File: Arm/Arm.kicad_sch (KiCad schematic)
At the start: 53 parts, among them J10 SparkMAX XT60 F, J11 CAN OUT, J12 Axis 0, J13 SparkMAX XT60 F, J14 Encoder 0, J2 Encoder Bundle, J3 CAN IN, J4 5V Swtich Power, J5 Power IN XT60 M, J6 SparkMAX XT60 F, J7 Power OUT XT60 F, J8 Lynx, J9 CANBUS, M1 Fan, U4 TJA1051T, U5 TJA1051T, U7 RASPBERRY_PI_4B_4GB

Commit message: URC '25 - V2
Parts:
- removed A1, A2: Adafruit_Feather_HUZZAH32_ESP32, Module:Adafruit_Feather, symbol Arm:Adafruit Feather ESP32 V2
- removed J12: Axis 0, Connector_Molex:Molex_Mini-Fit_Jr_5566-04A_2x02_P4.20mm_Vertical, symbol Connector:Conn_01x04_Pin
- removed U6: ~, Arm:Pololu 3730, symbol Arm:Pololu_3730
- added C7: 0.1 uF, Capacitor_SMD:C_0603_1608Metric_Pad1.08x0.95mm_HandSolder, symbol Device:C
- added D5: Inolux_IN-PI554FCH, LED_SMD:LED_Inolux_IN-PI554FCH_PLCC4_5.0x5.0mm_P3.2mm, symbol LED:Inolux_IN-PI554FCH
- added J12: SparkMAX XT60 F, Connector_AMASS:AMASS_XT60-F_1x02_P7.20mm_Vertical, symbol Connector:Conn_01x02_Pin
- added R16: 10K ohm, Resistor_SMD:R_0603_1608Metric_Pad0.98x0.95mm_HandSolder, symbol Device:R
- added U6, U8: ~, ESP 32 DOIT devkit V1:esp32_devkit_v1_doit, symbol ESP 32 DOIT devkit V1:ESP32_DOIT_devkit_V1
- J8: footprint Connector_Molex:Molex_Mini-Fit_Jr_5566-04A_2x02_P4.20mm_Vertical -> Connector_AMASS:AMASS_XT30U-F_1x02_P5.0mm_Vertical; symbol Connector:Conn_01x04_Pin -> Connector:Conn_01x02_Pin
- R5: value 3.8K Ohm -> 3.32K Ohm
- R7: value 3.1K Ohm -> 2.21K ohm
- U7: footprint Raspi:MODULE_RASPBERRY_PI_4B_4GB -> RASPBERRY_PI_4B_4GB:MODULE_RASPBERRY_PI_4B_4GB; Description_1 BCM2711 Raspberry Pi 4 Model B 4GB - ARM® Cortex®-A72 MPU Embedded Evaluation Board -> BCM2711 Raspberry Pi 4 Model B 4GB - ARM® Cortex®-A72 MPU Embedded Evaluation Board
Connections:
- net ESP_RX-LYNX_TX is gone; now on net +12V: J8.1 (Pin_1)
- net ESP_TX-LYNX_RX is gone; now on net GND: J8.2 (Pin_2)
- net +12V: no longer J8.3 (Pin_3)
- net +3.3V: now also R16.1; no longer R3.1
- net +5V: now also C7.1, D5.3 (VDD), U6.15 (VIN), U8.15 (VIN)
- net +BATT: now also J12.2 (Pin_2)
- net 12V_ADC: now also U6.2 (GPI36/A0)
- net 5V_ADC: now also U6.4 (GPI34/A6)
- net BATT_ADC: now also U6.3 (GPI39/A3)
- net CLK_ESP0: now also U6.24 (GPIO18/SCK)
- net CS_Encoder_0: now also J14.3 (Pin_3), U6.6 (GPIO32/A4); no longer J14.4 (Pin_4)
- net CS_Encoder_1: now also U6.7 (GPIO33/A5)
- net CS_Encoder_2: now also U6.8 (GPIO25/A18)
- net CS_Encoder_3: now also U6.9 (GPIO26/A19)
- net ESP0 3.3V: now also U6.16 (3.3V)
- net ESP0_ESP1_SERIAL: now also U6.21 (GPIO16/RX2), U8.22 (GPIO17/TX2)
- net ESP1 3.3V: now also U8.16 (3.3V)
- net ESP1_ESP0_SERIAL: now also U6.22 (GPIO17/TX2), U8.21 (GPIO16/RX2)
- net GND: now also J14.2 (Pin_2), C7.2, D5.1 (VSS), J12.1 (Pin_1), U6.14 (GND), U6.17 (GND), U8.14 (GND), U8.17 (GND); no longer J14.5 (Pin_5), J8.4 (Pin_4)
- net MISO_ESP0: now also J14.5 (Pin_5), U6.25 (GPIO19/MISO); no longer J14.3 (Pin_3)
- net MOSI_ESP0: now also J14.4 (Pin_4), U6.30 (GPIO23/MOSI); no longer J14.2 (Pin_2)
- net ESP0_RX-CAN_TX renamed ESP0_TX-CAN_TX
- net ESP0_TX-CAN_TX: now also U6.13 (GPIO13/A14)
- net ESP0_TX-CAN_RX renamed ESP0_RX-CAN_RX
- net ESP0_RX-CAN_RX: now also U6.11 (GPIO14/A16)
- net ESP1_RX-CAN_TX renamed ESP1_TX-CAN_TX
- net ESP1_TX-CAN_TX: now also U8.13 (GPIO13/A14)
- net ESP1_TX-CAN_RX renamed ESP1_RX-CAN_RX
- net ESP1_RX-CAN_RX: now also U8.11 (GPIO14/A16)
- new net 3.3V_ADC: R16.2, R3.1, U6.5 (GPI35/A7)
- new net LED Debug: D5.2 (DIN), U6.29 (GPIO22/SCL)
- no-connect marks 41 -> 73
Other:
- note added: "Status LED"
- note removed: "Axis 0 Motor Driver"
- note removed: "Stepper Motor Axis 0"
- note removed: "Supply 14.8V Max Current 1.5A"

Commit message: PCB Layout....
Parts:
- removed C2: 4.7 nf, Capacitor_SMD:C_0603_1608Metric_Pad1.08x0.95mm_HandSolder, symbol Device:C
- removed R12, R13: 60Ω, Resistor_SMD:R_0603_1608Metric_Pad0.98x0.95mm_HandSolder, symbol Device:R_Small_US
- removed U5: TJA1051T, Package_SO:SOIC-8_3.9x4.9mm_P1.27mm, symbol Interface_CAN_LIN:TJA1051T-3
- removed U6, U8: ~, ESP 32 DOIT devkit V1:esp32_devkit_v1_doit, symbol ESP 32 DOIT devkit V1:ESP32_DOIT_devkit_V1
- removed U7: RASPBERRY_PI_4B_4GB, RASPBERRY_PI_4B_4GB:MODULE_RASPBERRY_PI_4B_4GB, symbol RASPBERRY_PI_4B_4GB:RASPBERRY_PI_4B_4GB
- added C10, C8, C9: 0.1 uF, Capacitor_SMD:C_0603_1608Metric_Pad1.08x0.95mm_HandSolder, symbol Device:C
- added C11: 4.7 nF, Capacitor_SMD:C_0603_1608Metric_Pad1.08x0.95mm_HandSolder, symbol Device:C
- added R17, R18: 60Ω, Resistor_SMD:R_0603_1608Metric_Pad0.98x0.95mm_HandSolder, symbol Device:R_Small_US
- added U5: ESP32-S3-DevKitC, Astra Lib:ESP32-S3-DevKitC, symbol ESP32-S3-DevkitC:ESP32-S3-DevKitC
- added U9: MCP251863T-E-9PX, Package_DFN_QFN:VQFN-28-1EP_5x5mm_P0.5mm_EP3.25x3.25mm, symbol Interface_CAN_LIN:MCP251863T-E-9PX
- added Y3: 40Mhz Crystal, Crystal:Crystal_SMD_3225-4Pin_3.2x2.5mm, symbol Device:Crystal_GND23
- C4: value 1 uF -> 13 pF
- C6: value 0.1 uF -> 13 pF
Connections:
- net +5V: now also C10.2, U5.3 (CHIP_PU), U9.13 (VCC); no longer C4.1
- net 12V_ADC: now also U5.31 (GPIO0)
- net 3.3V_ADC: now also U5.13 (GPIO3/ADC1_CH2)
- net 5V_ADC: now also U5.40 (GPIO2/ADC1_CH1)
- net Arm Motor CAN+: now also R18.2, U9.17 (CANH)
- net Arm Motor CAN-: now also R17.1, U9.16 (CANL)
- net BATT_ADC: now also U5.41 (GPIO1/ADC1_CH0)
- net CLK_ESP0: now also U5.29 (GPIO48), U9.22 (SCK)
- net CS_Encoder_0: now also U5.34 (GPIO37)
- net CS_Encoder_1: now also U5.35 (GPIO38)
- net CS_Encoder_2: now also U5.30 (GPIO45)
- net CS_Encoder_3: now also U5.14 (GPIO46)
- net ESP0 3.3V: now also C8.1, C9.1, U5.1 (3V3), U5.2 (3V3), U9.14 (VIO), U9.26 (VDD)
- net ESP0_RX-CAN_RX: now also U5.7 (GPIO7/ADC1_CH6)
- net ESP0_TX-CAN_TX: now also U5.11 (GPIO18/ADC2_CH7)
- net GND: now also C4.1, C10.1, C11.1, C8.2, C9.2, U5.22 (GND), U5.23 (GND), U5.24 (GND), U5.44 (GND), U9.10 (GND), U9.7 (VSS), Y3.2, Y3.3; no longer C4.2
- net LED Debug: now also U5.27 (GPIO21)
- net MISO_ESP0: now also U5.28 (GPIO47), U9.23 (SDI)
- net MOSI_ESP0: now also U5.32 (GPIO35), U9.24 (SDO)
- net ESP1 3.3V: no longer names the net of C6.2
- net ESP1 3.3V: now also U9.4 (OSC2), Y3.1
- new net: C4.2, U9.5 (OSC1), Y3.4
- new net: C11.2, R17.2, R18.1
- new net: U9.1 (RXCAN), U9.11 (RXD)
- new net: U9.20 (TXD), U9.28 (TXCAN)
- new net CS_Motor_CAN: U5.33 (GPIO36), U9.25 (~{CS})
- no-connect marks 73 -> 14
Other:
- note added: "Main ESP"
- note removed: "Motor Control"
- note removed: "Nuc Control"
- note removed: "Raspberry Pi"
- moved on the sheet: C1, C3, C5, C7, D1, D2, D3, D4, D5, H1, H2, H3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

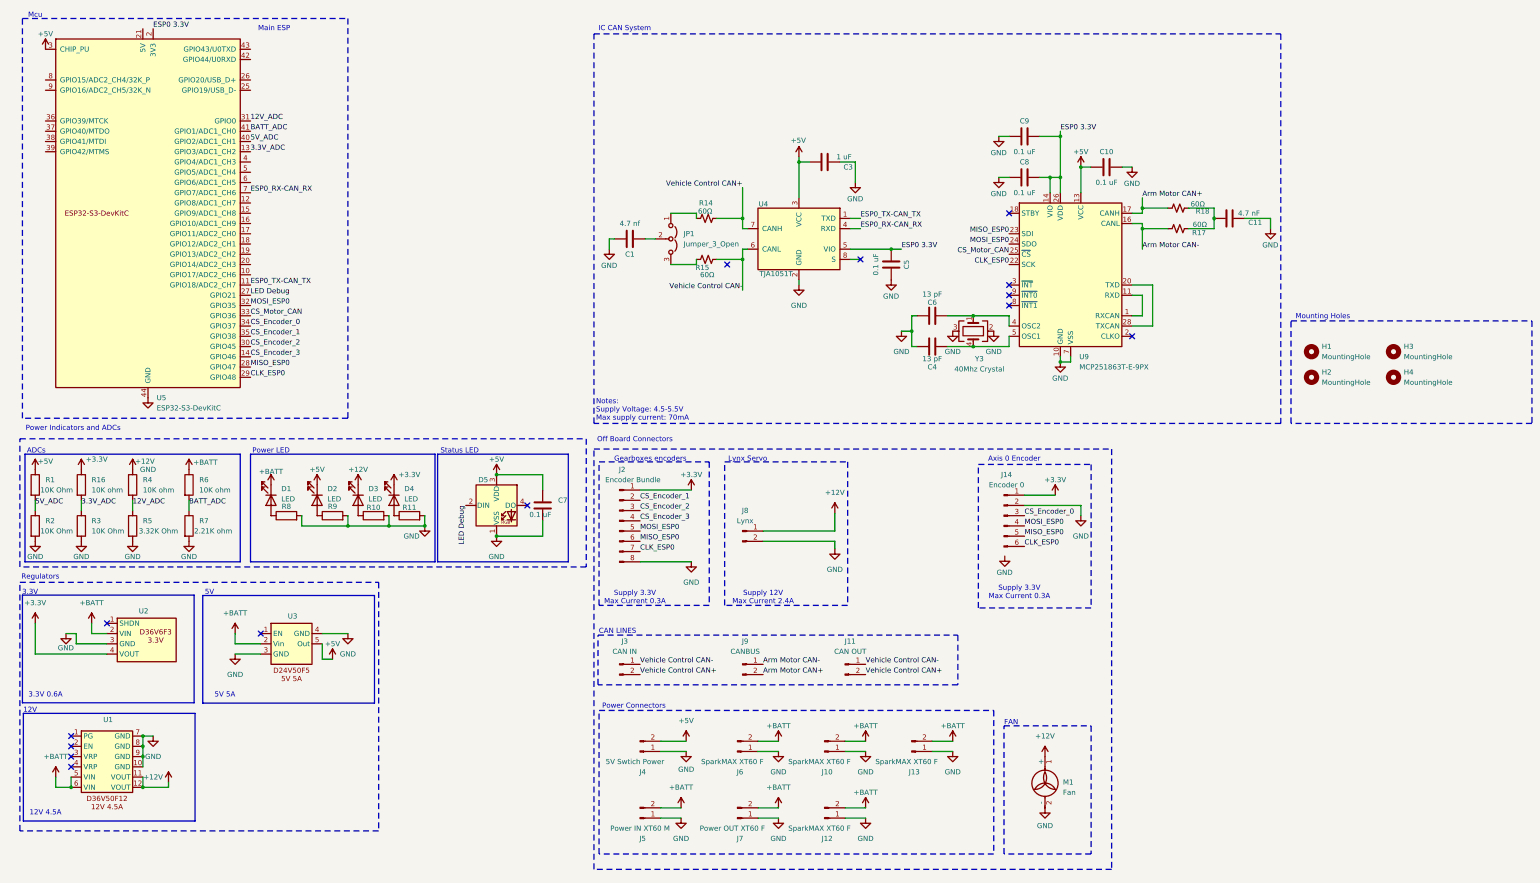
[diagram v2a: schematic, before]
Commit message: Progrss on socket -FeedBack Fixes -PCB Layout and signal routing
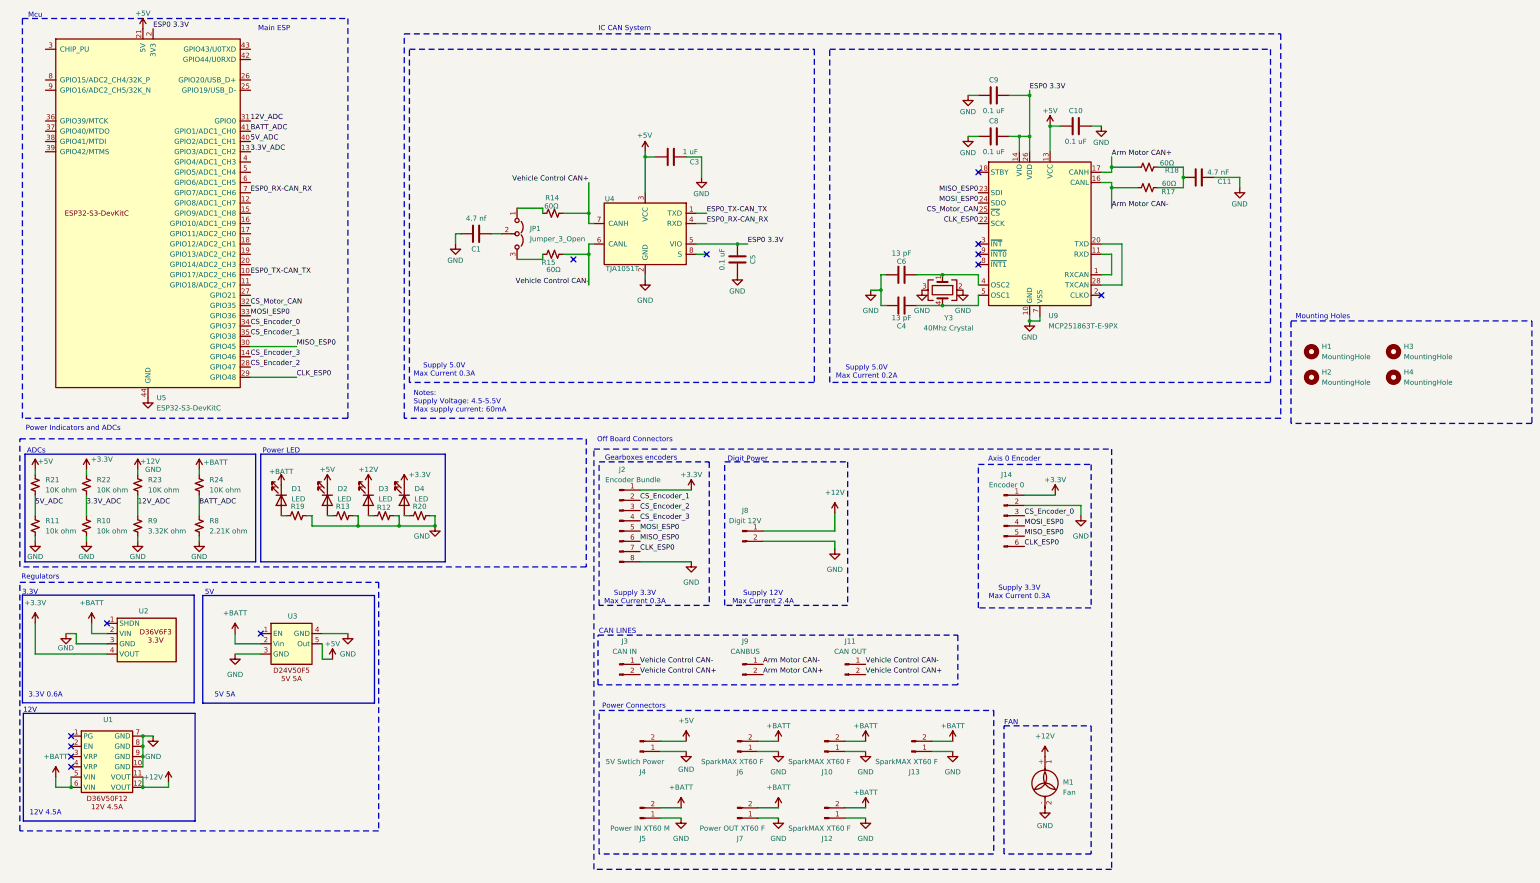
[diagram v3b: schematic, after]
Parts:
- removed C7: 0.1 uF, Capacitor_SMD:C_0603_1608Metric_Pad1.08x0.95mm_HandSolder, symbol Device:C
- removed D5: Inolux_IN-PI554FCH, LED_SMD:LED_Inolux_IN-PI554FCH_PLCC4_5.0x5.0mm_P3.2mm, symbol LED:Inolux_IN-PI554FCH
- removed R1, R2, R3: 10K Ohm, Resistor_SMD:R_0603_1608Metric_Pad0.98x0.95mm_HandSolder, symbol Device:R
- removed R10, R11, R8, R9: 3.8K Ohm, Resistor_SMD:R_0603_1608Metric_Pad0.98x0.95mm_HandSolder, symbol Device:R
- removed R16, R4, R6: 10K ohm, Resistor_SMD:R_0603_1608Metric_Pad0.98x0.95mm_HandSolder, symbol Device:R
- removed R5: 3.32K Ohm, Resistor_SMD:R_0603_1608Metric_Pad0.98x0.95mm_HandSolder, symbol Device:R
- removed R7: 2.21K ohm, Resistor_SMD:R_0603_1608Metric_Pad0.98x0.95mm_HandSolder, symbol Device:R
- added R10, R11: 10k ohm, Resistor_SMD:R_0603_1608Metric_Pad0.98x0.95mm_HandSolder, symbol Device:R_Small_US
- added R12, R13, R20: R_Small_US, Resistor_SMD:R_0603_1608Metric_Pad0.98x0.95mm_HandSolder, symbol Device:R_Small_US
- added R19: 2k ohm, Resistor_SMD:R_0603_1608Metric_Pad0.98x0.95mm_HandSolder, symbol Device:R_Small_US
- added R21, R22, R23, R24: 10K ohm, Resistor_SMD:R_0603_1608Metric_Pad0.98x0.95mm_HandSolder, symbol Device:R_Small_US
- added R8: 2.21K ohm, Resistor_SMD:R_0603_1608Metric_Pad0.98x0.95mm_HandSolder, symbol Device:R_Small_US
- added R9: 3.32K ohm, Resistor_SMD:R_0603_1608Metric_Pad0.98x0.95mm_HandSolder, symbol Device:R_Small_US
- J11, J3: footprint Connector_AMASS:AMASS_XT30U-M_1x02_P5.0mm_Vertical -> Connector_AMASS:AMASS_XT30PW-M_1x02_P2.50mm_Horizontal
- J8: value Lynx -> Digit 12V; footprint Connector_AMASS:AMASS_XT30U-F_1x02_P5.0mm_Vertical -> Connector_AMASS:AMASS_XT30PW-F_1x02_P2.50mm_Horizontal
- J9: footprint Connector_AMASS:AMASS_XT30U-F_1x02_P5.0mm_Vertical -> Connector_AMASS:AMASS_XT30PW-F_1x02_P2.50mm_Horizontal
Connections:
- net +12V: now also R23.1
- net +3.3V: now also R22.1
- net +5V: now also U5.21 (5V), R21.1; no longer U5.3 (CHIP_PU)
- net +BATT: now also R24.1
- net 12V_ADC: now also R23.2, R9.1
- net 3.3V_ADC: now also R10.1, R22.2
- net 5V_ADC: now also R11.1, R21.2
- net BATT_ADC: now also R24.2, R8.1
- net CS_Encoder_2: now also U5.28 (GPIO47); no longer U5.30 (GPIO45)
- net CS_Motor_CAN: now also U5.32 (GPIO35); no longer U5.33 (GPIO36)
- net ESP0_TX-CAN_TX: now also U5.10 (GPIO17/ADC2_CH6); no longer U5.11 (GPIO18/ADC2_CH7)
- net GND: now also R10.2, R11.2, R12.2, R13.2, R19.2, R20.2, R8.2, R9.2
- net MISO_ESP0: now also U5.30 (GPIO45); no longer U5.28 (GPIO47)
- net MOSI_ESP0: now also U5.33 (GPIO36); no longer U5.32 (GPIO35)
- net at D4.2 (A): now also R20.1
- net at D1.2 (A): now also R19.1
- net at D3.2 (A): now also R12.1
- net at D2.2 (A): now also R13.1
- net LED Debug: no longer names the net of U5.27 (GPIO21)
- no-connect marks 14 -> 13
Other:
- note added: "Digit Power"
- note added: "Notes: Supply Voltage: 4.5-5.5V Max supply current: 60mA"
- note added: "Supply 5.0V Max Current 0.2A"
- note added: "Supply 5.0V Max Current 0.3A"
- note removed: "Lynx Servo"
- note removed: "Notes: Supply Voltage: 4.5-5.5V Max supply current: 70mA"
- note removed: "Status LED"
- moved on the sheet: C1, C10, C11, C3, C4, C5, C6, C8, C9, D1, D2, D3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

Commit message: More Work on PCB
Moved some stuff around
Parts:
- removed D2, D3, D4: LED, LED_SMD:LED_0603_1608Metric_Pad1.05x0.95mm_HandSolder, symbol Device:LED
- added D5, D6, D7: LED, LED_SMD:LED_0603_1608Metric_Pad1.05x0.95mm_HandSolder, symbol Device:LED
- J10: footprint Connector_AMASS:AMASS_XT60-F_1x02_P7.20mm_Vertical -> Connector_AMASS:AMASS_XT60-M_1x02_P7.20mm_Vertical
- J11, J3: footprint Connector_AMASS:AMASS_XT30PW-M_1x02_P2.50mm_Horizontal -> Connector_AMASS:AMASS_XT30U-F_1x02_P5.0mm_Vertical
- J12, J6, J7: footprint Connector_AMASS:AMASS_XT60-F_1x02_P7.20mm_Vertical -> Connector_AMASS:AMASS_XT60PW-F_1x02_P7.20mm_Horizontal
- J5: footprint Connector_AMASS:AMASS_XT60-M_1x02_P7.20mm_Vertical -> Connector_AMASS:AMASS_XT60PW-M_1x02_P7.20mm_Horizontal
- J9: footprint Connector_AMASS:AMASS_XT30PW-F_1x02_P2.50mm_Horizontal -> Connector_AMASS:AMASS_XT30U-F_1x02_P5.0mm_Vertical
- U9: footprint Package_DFN_QFN:VQFN-28-1EP_5x5mm_P0.5mm_EP3.25x3.25mm -> Package_SO:SSOP-28_5.3x10.2mm_P0.65mm
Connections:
- net +12V: now also D6.2 (A)
- net +3.3V: now also D7.2 (A)
- net +5V: now also D1.2 (A)
- net +BATT: now also D5.2 (A); no longer D1.1 (K)
- net 12V_ADC: now also U5.16 (GPIO10/ADC1_CH9); no longer U5.31 (GPIO0)
- net at R19.1: now also D5.1 (K); no longer D1.2 (A)
- net at R20.1: now also D7.1 (K)
- net at R12.1: now also D6.1 (K)
- net at R13.1: now also D1.1 (K)
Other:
- moved on the sheet: R12, R13, R19, R20

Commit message: So Close...
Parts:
- J8: footprint Connector_AMASS:AMASS_XT30PW-F_1x02_P2.50mm_Horizontal -> Connector_AMASS:AMASS_XT30U-F_1x02_P5.0mm_Vertical
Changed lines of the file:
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@@
 			)
 		)
-		(property "Footprint" "Connector_AMASS:AMASS_XT30PW-F_1x02_P2.50mm_Horizontal"
+		(property "Footprint" "Connector_AMASS:AMASS_XT30U-F_1x02_P5.0mm_Vertical"
 			(at 195.58 142.24 0)
 			(effects

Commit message: Had the plague
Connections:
- net ESP0_RX-CAN_RX: now also U5.4 (GPIO4/ADC1_CH3); no longer U5.7 (GPIO7/ADC1_CH6)
- net ESP0_TX-CAN_TX: now also U5.5 (GPIO5/ADC1_CH4); no longer U5.10 (GPIO17/ADC2_CH6)
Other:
- note added: "Supply 12V Max Current 3A?"
- note added: "Supply 3.3V Max Current 1A?"
- note added: "Supply 5.0V Max Current 0.2A(Should be 0.02A)"
- note removed: "Supply 12V Max Current 2.4A"
- note removed: "Supply 5.0V Max Current 0.2A"
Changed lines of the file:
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@@
 		)
 	)
-	(text "Supply 5.0V\nMax Current 0.2A"
+	(text "Supply 5.0V\nMax Current 0.2A(Should be 0.02A)"
 		(exclude_from_sim no)
-		(at 226.314 102.87 0)
+		(at 218.44 102.87 0)
 		(effects
 			(font
 				(size 1.27 1.27)
 			)
+			(justify left)
 		)
 	)
@@
 		)
 	)
-	(text "Supply 3.3V\nMax Current 0.3A"
+	(text "Supply 3.3V\nMax Current 1A?"
 		(exclude_from_sim no)
 		(at 168.91 158.75 0)
@@
 		)
 	)
-	(text "Supply 12V\nMax Current 2.4A"
+	(text "Supply 12V\nMax Current 3A?"
 		(exclude_from_sim no)
 		(at 200.66 158.75 0)
@@
 		)
 	)
+	(label "ESP0_RX-CAN_RX"
+		(at 73.66 50.8 0)
+		(effects
+			(font
+				(size 1.27 1.27)
+			)
+			(justify left bottom)
+		)
+	)
 	(label "Arm Motor CAN+"
 		(at 200.66 177.8 0)
@@
 		)
 	)
-	(label "ESP0_RX-CAN_RX"
-		(at 73.66 58.42 0)
-		(effects
-			(font
-				(size 1.27 1.27)
-			)
-			(justify left bottom)
-		)
-	)
 	(label "MOSI_ESP0"
 		(at 265.43 140.97 0)
@@
 		)
 	)
+	(label "ESP0_TX-CAN_TX"
+		(at 73.66 53.34 0)
+		(effects
+			(font
+				(size 1.27 1.27)
+			)
+			(justify left bottom)
+		)
+	)
 	(label "CLK_ESP0"
 		(at 265.43 146.05 0)
@@
 		)
 	)
-	(label "ESP0_TX-CAN_TX"
-		(at 73.66 78.74 0)
-		(effects
-			(font
-				(size 1.27 1.27)
-			)
-			(justify left bottom)
-		)
-	)
 	(label "5V_ADC"
 		(at 20.32 135.89 0)
@@
 			)
 		)
-		(property "Datasheet" ""
+		(property "Datasheet" "https://www.pololu.com/product/4095"
 			(at 38.1 190.5 0)
 			(effects
@@
 			)
 		)
-		(property "Datasheet" ""
+		(property "Datasheet" "https://www.pololu.com/product/3791"
 			(at 43.18 162.56 0)
 			(effects
@@
 			)
 		)
-		(property "Datasheet" ""
+		(property "Datasheet" "https://www.pololu.com/product/2851"
 			(at 83.82 163.83 0)
 			(effects

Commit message: 1 PCB 2 PCB 3 PCB ...
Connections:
- net 5V_ADC: now also U5.6 (GPIO6/ADC1_CH5); no longer U5.40 (GPIO2/ADC1_CH1)
- net CS_Encoder_2: now also U5.4 (GPIO4/ADC1_CH3); no longer U5.28 (GPIO47)
- net ESP0_RX-CAN_RX: now also U5.11 (GPIO18/ADC2_CH7); no longer U5.4 (GPIO4/ADC1_CH3)
- net ESP0_TX-CAN_TX: now also U5.10 (GPIO17/ADC2_CH6); no longer U5.5 (GPIO5/ADC1_CH4)
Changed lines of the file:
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@@
-		)
-	)
-	(label "ESP0_RX-CAN_RX"
-		(at 73.66 50.8 0)
-		(effects
-			(font
-				(size 1.27 1.27)
-			)
-			(justify left bottom)
 		)
 	)
@@
 		)
 	)
+	(label "CS_Encoder_2"
+		(at 73.66 50.8 0)
+		(effects
+			(font
+				(size 1.27 1.27)
+			)
+			(justify left bottom)
+		)
+	)
 	(label "ESP0_RX-CAN_RX"
 		(at 186.69 66.04 0)
@@
 		)
 	)
+	(label "ESP0_TX-CAN_TX"
+		(at 73.66 78.74 0)
+		(effects
+			(font
+				(size 1.27 1.27)
+			)
+			(justify left bottom)
+		)
+	)
 	(label "CS_Motor_CAN"
 		(at 73.66 86.36 0)
@@
 		)
 	)
+	(label "ESP0_RX-CAN_RX"
+		(at 73.66 81.28 0)
+		(effects
+			(font
+				(size 1.27 1.27)
+			)
+			(justify left bottom)
+		)
+	)
 	(label "ESP0 3.3V"
 		(at 266.7 33.02 0)
@@
 		)
 	)
+	(label "5V_ADC"
+		(at 73.66 55.88 0)
+		(effects
+			(font
+				(size 1.27 1.27)
+			)
+			(justify left bottom)
+		)
+	)
 	(label "MISO_ESP0"
 		(at 85.09 96.52 0)
@@
 	)
 	(label "CS_Encoder_2"
-		(at 73.66 101.6 0)
-		(effects
-			(font
-				(size 1.27 1.27)
-			)
-			(justify left bottom)
-		)
-	)
-	(label "CS_Encoder_2"
 		(at 170.18 137.16 0)
 		(effects
@@
 		)
 	)
-	(label "ESP0_TX-CAN_TX"
-		(at 73.66 53.34 0)
-		(effects
-			(font
-				(size 1.27 1.27)
-			)
-			(justify left bottom)
-		)
-	)
 	(label "CLK_ESP0"
 		(at 265.43 146.05 0)
@@
 		(effects
 			(font
-				(size 1.27 1.27)
-			)
-			(justify left bottom)
-		)
-	)
-	(label "5V_ADC"
-		(at 73.66 45.72 0)
-		(effects
-			(font

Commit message: Changes were mostly traces and part spacing
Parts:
- H1, H2, H3, H4: footprint Arm:4-40 Mounting Hole -> MountingHole:MountingHole_3.2mm_M3
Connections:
- net CS_Encoder_3: now also U5.7 (GPIO7/ADC1_CH6); no longer U5.14 (GPIO46)
